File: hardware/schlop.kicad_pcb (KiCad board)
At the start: 2 copper layers, 141.5 x 119.4 mm, 43 parts, among them SW1 SW_SPST, SW10 SW_SPST, SW11 SW_SPST, SW12 SW_SPST, SW13 SW_SPST, SW14 SW_SPST, SW15 SW_SPST, SW16 SW_SPST, SW17 SW_SPST, SW18 SW_SPST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

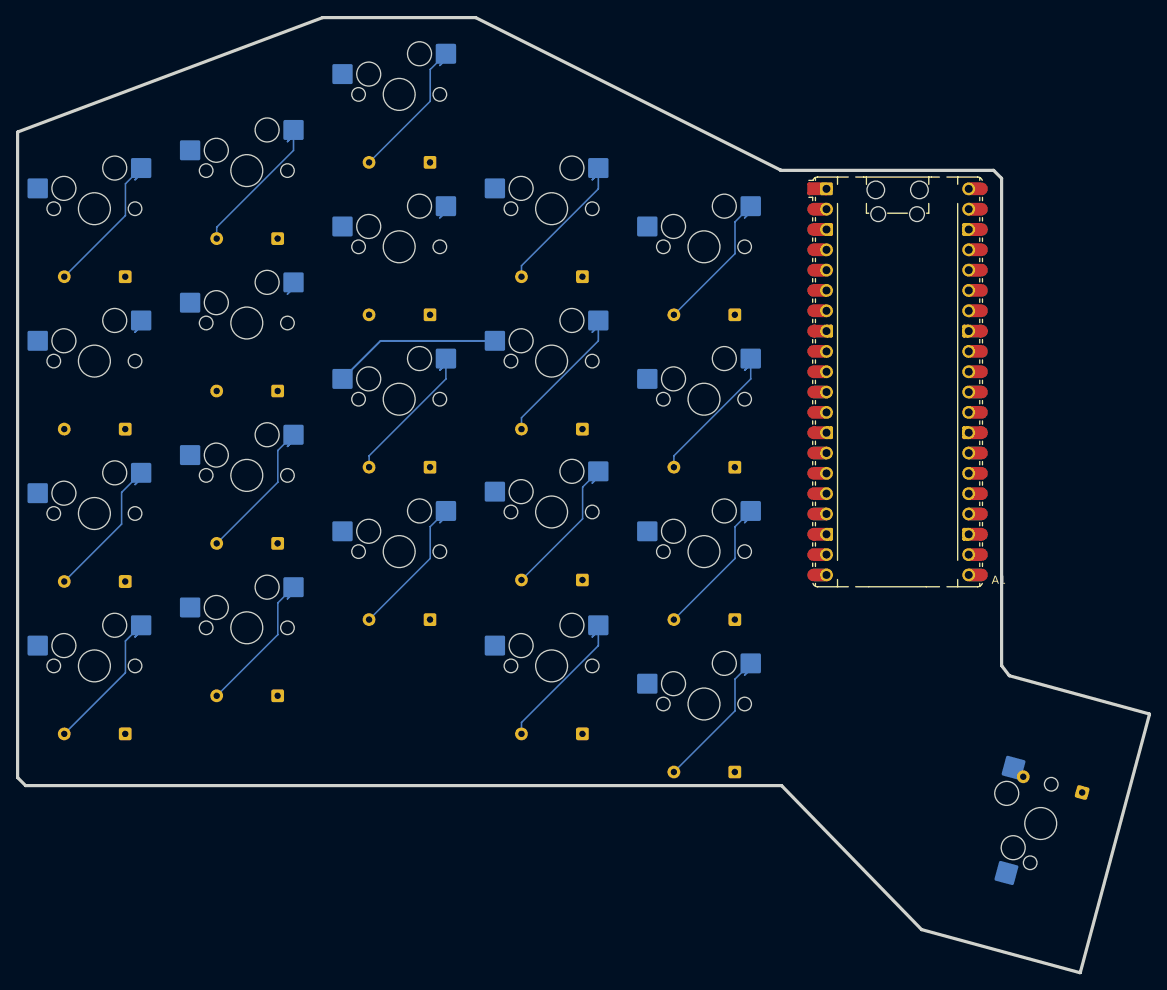
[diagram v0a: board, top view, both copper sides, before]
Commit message: finished pcb routing and mounting
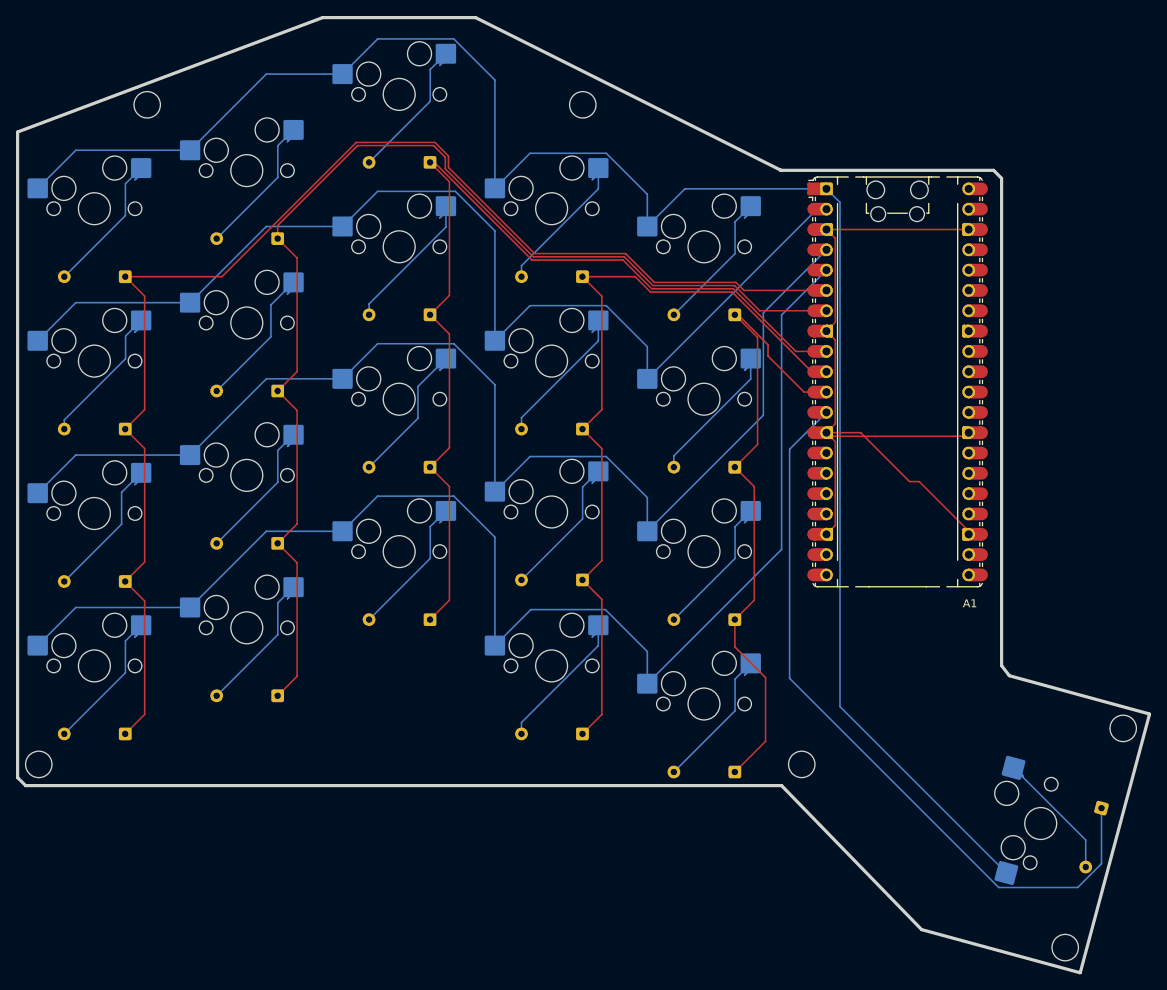
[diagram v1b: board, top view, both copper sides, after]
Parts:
- moved SW16 57.1 mm to (38.1, 109.5)
- moved SW19 57.1 mm to (95.2, 109.5)
- moved D21 3.11 mm to (164.0, 127.3), turned to -105 degrees
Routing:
- net Net-(A1-GPIO0): track 42.0 -> 226.7 mm
- net Net-(A1-GPIO3): track 0.00 -> 168.6 mm
- net Net-(A1-GPIO4): track 0.00 -> 166.3 mm
- net Net-(A1-GPIO2): track 0.00 -> 152.0 mm
- net Net-(A1-GPIO5): track 0.00 -> 146.9 mm
- net Net-(A1-GPIO1): track 0.00 -> 138.5 mm
- net Net-(A1-GPIO6): track 0.00 -> 122.5 mm
- net Net-(A1-GPIO7): track 0.00 -> 100.9 mm
- net GND: track 0.00 -> 100.8 mm
- net Net-(A1-GPIO9): track 0.00 -> 93.1 mm
- net Net-(A1-GPIO8): track 0.00 -> 80.2 mm
- net Net-(D19-A): track 0.00 -> 21.1 mm
- net Net-(D15-A): track 42.2 -> 21.1 mm
- net Net-(D16-A): track 0.00 -> 21.1 mm
- net Net-(D10-A): track 42.2 -> 21.1 mm
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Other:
- outline, holes or cut-outs redrawn
